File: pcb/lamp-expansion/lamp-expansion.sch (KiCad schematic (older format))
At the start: 87 parts, among them IC1 PAM2421, IC2 MCP73811, IC3 AP2401, IC6 LM1117_5.0, IC7 FT230X_SOP, IC9 CC3000, J1 MICROUSB, J10 CC-IO, J2 DCIN, J3 SERIAL, J4 5PIN_INPUT, J5 2PIN_POWER, J6 2PIN_IO, J7 2PIN_POWER, J8 AVR_ISP, J9 UF.L, Q1 2N7002

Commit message: board layout and schematic refinement
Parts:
- removed C10, C2: 0.1uF, symbol C
- removed IC3: AP2401, symbol AP24x1
- removed J10: CC-IO, symbol 3PIN_FEMALE
- removed J6: 2PIN_IO, symbol 2PIN_FEMALE
- removed R1: 10kΩ, symbol R
- removed TP11, TP12: PIN, symbol TEST
- added Q?: AO3415, symbol P-CHAN-MOSFET_SOT
- added R?: 100kΩ, symbol R
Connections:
- net labels removed: +BATT, AVR_0, AVR_1
- wire segments 255 -> 305
- no-connect marks 4 -> 3
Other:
- note added: "communication headers"
- note removed: "battery and charger"
- note removed: "buttons and pots header"
- note removed: "extra io"
- note removed: "power switch"
- note removed: "wifi io pins"
- moved on the sheet: BT1, C1, C9, D1, IC2, J4, R10, R11, S1, S2, TP10, TP6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

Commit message: a little more room fort activities
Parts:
- removed D1: 3A, symbol D_SCHOTTKY
- removed JP2: I-TEST, symbol JUMPER_2-PIN
- removed Q?: AO3415, symbol P-CHAN-MOSFET_SOT
- added IC3: NTHD3101F, symbol NTHD3101F
- gave numbers to parts that had none: 1
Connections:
- net +5V: now also IC3.1 (A), IC3.2 (A), IC3.4 (G)
- net VSUP: now also IC3.3 (S), IC3.7 (C), IC3.8 (C)
- net at BT1.1 (+), C9.1, IC2.3 (VBAT): now also IC3.5 (D), IC3.6 (D)
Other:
- moved on the sheet: J7, R1

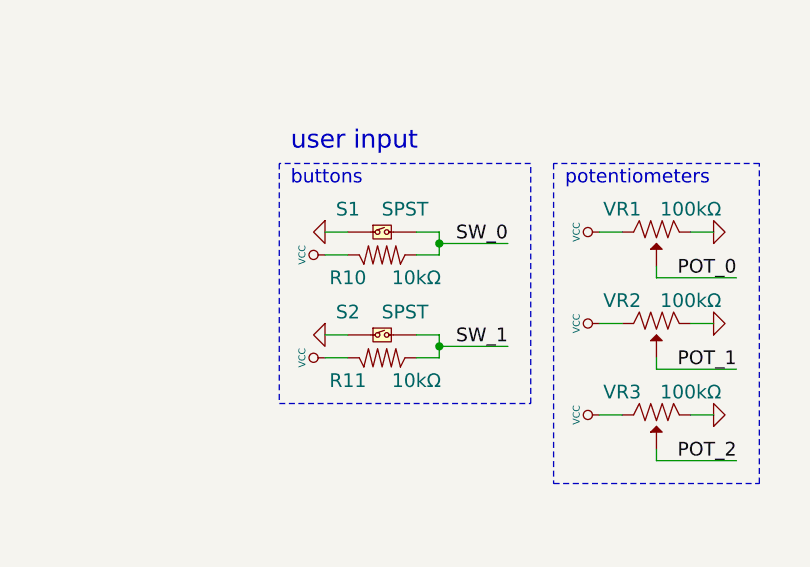
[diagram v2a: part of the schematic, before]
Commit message: layout and schematic refinements
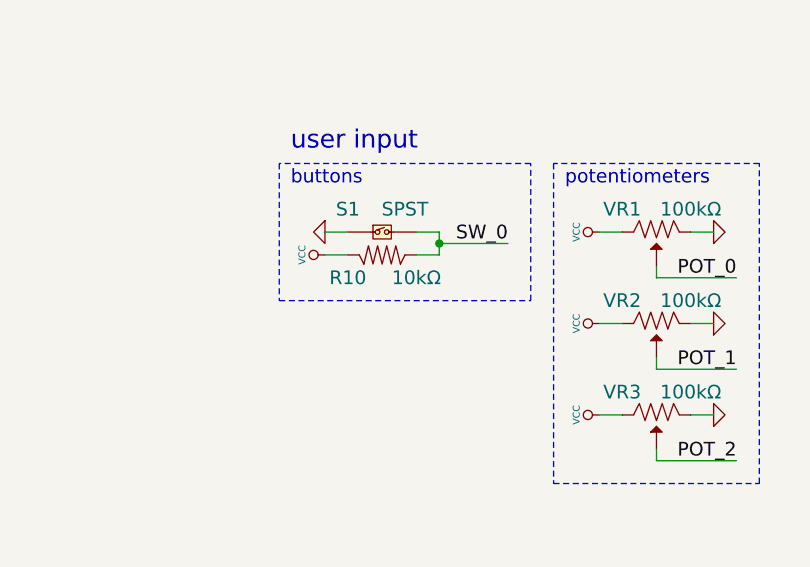
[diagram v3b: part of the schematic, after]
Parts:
- removed R11: 10kΩ, symbol R
- removed S2: SPST, symbol SPST
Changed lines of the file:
@@
 Text Label 8200 3700 2    60   ~ 0
 SW_0
-$Comp
-L SPST S2
-U 1 1 5358ABCF
-P 7650 4100
-F 0 "S2" H 7500 4200 60  0000 C CNN
-F 1 "SPST" H 7750 4200 60  0000 C CNN
-F 2 "" H 7650 4100 60  0001 C CNN
-F 3 "" H 7650 4100 60  0001 C CNN
-	1    7650 4100
-	1    0    0    -1
-$EndComp
-$Comp
-L GND #PWR046
-U 1 1 5358ABD5
-P 7400 4100
-F 0 "#PWR046" H 7400 4100 30  0001 C CNN
-F 1 "GND" H 7400 4030 30  0001 C CNN
-F 2 "" H 7400 4100 60  0000 C CNN
-F 3 "" H 7400 4100 60  0000 C CNN
-	1    7400 4100
-	0    1    1    0
-$EndComp
-$Comp
-L R R11
-U 1 1 5358ABDC
-P 7650 4200
-F 0 "R11" H 7500 4100 60  0000 C CNN
-F 1 "10kΩ" H 7800 4100 60  0000 C CNN
-F 2 "" H 7650 4200 60  0001 C CNN
-F 3 "" H 7650 4200 60  0001 C CNN
-	1    7650 4200
-	1    0    0    -1
-$EndComp
-$Comp
-L VCC #PWR047
-U 1 1 5358ABE2
-P 7400 4200
-F 0 "#PWR047" H 7400 4300 30  0001 C CNN
-F 1 "VCC" H 7400 4300 30  0000 C CNN
-F 2 "" H 7400 4200 60  0000 C CNN
-F 3 "" H 7400 4200 60  0000 C CNN
-	1    7400 4200
-	0    -1   -1   0
-$EndComp
-Text Label 8200 4150 2    60   ~ 0
-SW_1
 Text Notes 8450 3450 0    60   ~ 0
 potentiometers
@@
 $EndComp
 $Comp
-L PWR_FLAG #FLG048
+L PWR_FLAG #FLG046
 U 1 1 53613807
 P 3150 8950
-F 0 "#FLG048" H 3150 9045 30  0001 C CNN
+F 0 "#FLG046" H 3150 9045 30  0001 C CNN
 F 1 "PWR_FLAG" H 3150 9130 30  0000 C CNN
 F 2 "" H 3150 8950 60  0000 C CNN
@@
 $EndComp
 $Comp
-L PWR_FLAG #FLG049
+L PWR_FLAG #FLG047
 U 1 1 53613C3F
 P 7950 1550
-F 0 "#FLG049" H 7950 1645 30  0001 C CNN
+F 0 "#FLG047" H 7950 1645 30  0001 C CNN
 F 1 "PWR_FLAG" H 7950 1730 30  0000 C CNN
 F 2 "" H 7950 1550 60  0000 C CNN
@@
 $EndComp
 $Comp
-L PWR_FLAG #FLG050
+L PWR_FLAG #FLG048
 U 1 1 5361446B
 P 1900 4500
-F 0 "#FLG050" H 1900 4595 30  0001 C CNN
+F 0 "#FLG048" H 1900 4595 30  0001 C CNN
 F 1 "PWR_FLAG" H 1900 4680 30  0000 C CNN
 F 2 "" H 1900 4500 60  0000 C CNN
@@
 $EndComp
 $Comp
-L GND #PWR051
+L GND #PWR049
 U 1 1 5363359C
 P 2150 6550
-F 0 "#PWR051" H 2150 6550 30  0001 C CNN
+F 0 "#PWR049" H 2150 6550 30  0001 C CNN
 F 1 "GND" H 2150 6480 30  0001 C CNN
 F 2 "" H 2150 6550 60  0000 C CNN
@@
 $EndComp
 $Comp
-L GND #PWR052
+L GND #PWR050
 U 1 1 53634DCF
 P 1950 7150
-F 0 "#PWR052" H 1950 7150 30  0001 C CNN
+F 0 "#PWR050" H 1950 7150 30  0001 C CNN
 F 1 "GND" H 1950 7080 30  0001 C CNN
 F 2 "" H 1950 7150 60  0000 C CNN
@@
 $EndComp
 $Comp
-L GND #PWR053
+L GND #PWR051
 U 1 1 53635854
 P 2300 7550
-F 0 "#PWR053" H 2300 7550 30  0001 C CNN
+F 0 "#PWR051" H 2300 7550 30  0001 C CNN
 F 1 "GND" H 2300 7480 30  0001 C CNN
 F 2 "" H 2300 7550 60  0000 C CNN
@@
 $EndComp
 $Comp
-L GND #PWR054
+L GND #PWR052
 U 1 1 53635980
 P 3100 7550
-F 0 "#PWR054" H 3100 7550 30  0001 C CNN
+F 0 "#PWR052" H 3100 7550 30  0001 C CNN
 F 1 "GND" H 3100 7480 30  0001 C CNN
 F 2 "" H 3100 7550 60  0000 C CNN
@@
 $EndComp
 $Comp
-L GND #PWR055
+L GND #PWR053
 U 1 1 536399D8
 P 3900 6750
-F 0 "#PWR055" H 3900 6750 30  0001 C CNN
+F 0 "#PWR053" H 3900 6750 30  0001 C CNN
 F 1 "GND" H 3900 6680 30  0001 C CNN
 F 2 "" H 3900 6750 60  0000 C CNN
@@
 $EndComp
 $Comp
-L GND #PWR056
+L GND #PWR054
 U 1 1 5363BCDD
 P 3600 7150
-F 0 "#PWR056" H 3600 7150 30  0001 C CNN
+F 0 "#PWR054" H 3600 7150 30  0001 C CNN
 F 1 "GND" H 3600 7080 30  0001 C CNN
 F 2 "" H 3600 7150 60  0000 C CNN
@@
 $EndComp
 $Comp
-L GND #PWR057
+L GND #PWR055
 U 1 1 5363C419
 P 1400 6250
-F 0 "#PWR057" H 1400 6250 30  0001 C CNN
+F 0 "#PWR055" H 1400 6250 30  0001 C CNN
 F 1 "GND" H 1400 6180 30  0001 C CNN
 F 2 "" H 1400 6250 60  0000 C CNN
@@
 	7900 3650 7900 3750
 Connection ~ 7900 3700
-Wire Wire Line
-	7400 4100 7500 4100
-Wire Wire Line
-	7400 4200 7500 4200
-Wire Wire Line
-	8200 4150 7900 4150
-Wire Wire Line
-	7900 4100 7800 4100
-Wire Wire Line
-	7900 4200 7800 4200
-Wire Wire Line
-	7900 4100 7900 4200
-Connection ~ 7900 4150
 Wire Notes Line
 	8400 3350 8400 4750
@@
 	9300 3350 8400 3350
 Wire Notes Line
-	7200 3350 7200 4400
-Wire Notes Line
-	7200 4400 8300 4400
-Wire Notes Line
-	8300 4400 8300 3350
+	7200 3350 7200 3950
+Wire Notes Line
+	7200 3950 8300 3950
+Wire Notes Line
+	8300 3950 8300 3350
 Wire Notes Line
 	8300 3350 7200 3350
@@
 	5300 7000 5200 7000
 $Comp
-L VCC #PWR058
+L VCC #PWR056
 U 1 1 53649906
 P 14700 4100
-F 0 "#PWR058" H 14700 4200 30  0001 C CNN
+F 0 "#PWR056" H 14700 4200 30  0001 C CNN
 F 1 "VCC" H 14700 4200 30  0000 C CNN
 F 2 "" H 14700 4100 60  0000 C CNN
@@
 NoConn ~ 11600 6200
 $Comp
-L GND #PWR059
+L GND #PWR057
 U 1 1 5364A71C
 P 12600 6200
-F 0 "#PWR059" H 12600 6200 30  0001 C CNN
+F 0 "#PWR057" H 12600 6200 30  0001 C CNN
 F 1 "GND" H 12600 6130 30  0001 C CNN
 F 2 "" H 12600 6200 60  0000 C CNN
@@
 $EndComp
 $Comp
-L PWR_FLAG #FLG060
+L PWR_FLAG #FLG058
 U 1 1 5364FF84
 P 3050 4850
-F 0 "#FLG060" H 3050 4945 30  0001 C CNN
+F 0 "#FLG058" H 3050 4945 30  0001 C CNN
 F 1 "PWR_FLAG" H 3050 5030 30  0000 C CNN
 F 2 "" H 3050 4850 60  0000 C CNN
@@
 Connection ~ 3050 4750
 $Comp
-L PWR_FLAG #FLG061
+L PWR_FLAG #FLG059
 U 1 1 53651E8C
 P 7250 9600
-F 0 "#FLG061" H 7250 9695 30  0001 C CNN
+F 0 "#FLG059" H 7250 9695 30  0001 C CNN
 F 1 "PWR_FLAG" H 7250 9780 30  0000 C CNN
 F 2 "" H 7250 9600 60  0000 C CNN
@@
 $EndComp
 $Comp
-L PWR_FLAG #FLG062
+L PWR_FLAG #FLG060
 U 1 1 536B0BCA
 P 9200 1550
-F 0 "#FLG062" H 9200 1645 30  0001 C CNN
+F 0 "#FLG060" H 9200 1645 30  0001 C CNN
 F 1 "PWR_FLAG" H 9200 1730 30  0000 C CNN
 F 2 "" H 9200 1550 60  0000 C CNN
@@
 $EndComp
 $Comp
-L +5V #PWR063
+L +5V #PWR061
 U 1 1 536ABC20
 P 3850 2150
-F 0 "#PWR063" H 3850 2240 20  0001 C CNN
+F 0 "#PWR061" H 3850 2240 20  0001 C CNN
 F 1 "+5V" H 3850 2240 30  0000 C CNN
 F 2 "" H 3850 2150 60  0000 C CNN
@@
 Connection ~ 3800 2150
 $Comp
-L +5V #PWR064
+L +5V #PWR062
 U 1 1 536AC23F
 P 3850 1600
-F 0 "#PWR064" H 3850 1690 20  0001 C CNN
+F 0 "#PWR062" H 3850 1690 20  0001 C CNN
 F 1 "+5V" H 3850 1690 30  0000 C CNN
 F 2 "" H 3850 1600 60  0000 C CNN
@@
 	3700 1900 4100 1900
 $Comp
-L GND #PWR065
+L GND #PWR063
 U 1 1 536AD142
 P 3300 1600
-F 0 "#PWR065" H 3300 1600 30  0001 C CNN
+F 0 "#PWR063" H 3300 1600 30  0001 C CNN
 F 1 "GND" H 3300 1530 30  0001 C CNN
 F 2 "" H 3300 1600 60  0000 C CNN

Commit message: still working on the layout
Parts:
- VR1, VR2, VR3: Distrib. Part (none) -> PTA2043-2015CPB103-ND; Distributor (none) -> Digikey; Manuf. Part (none) -> PTA2043-2015CPB103; Manufacturer (none) -> Bourns

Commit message: add changes found after first iMac powerup since 2014
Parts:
- AE1: footprint (none) -> johanson:JOHANSON-2500AT44M0400_2.4GHz-chip-antenna
- BT1: footprint (none) -> connect-thru:JST-S2B-PH-K_right-angle-jack
- C1, C14, C15, C16, C18, C22, C24, C26, C27, C28, C29, C30, C4, C5, C6, C9, L2, L3, R1, R10, R12, R13, R2, R4, R5, R6, R7, R8, R9: footprint (none) -> passive-smd:0603(1608m)
- C13, C20, C31, C7, C8, F1: footprint (none) -> passive-smd:1206(3216m)
- C19, C3: footprint (none) -> capacitor:PANA-D_CHEMI-F_SM-ALUMINUM
- D2, D6: footprint (none) -> diode:MICROSMP
- D3, D4: footprint (none) -> diode:DO-214AC
- IC1: footprint (none) -> sop:SOP8_ep
- IC2: footprint (none) -> sot:SOT23-5
- IC3: footprint (none) -> sot:CHIPFET-1206-8
- IC6: footprint (none) -> sot:SOT223
- IC7: footprint (none) -> sop:SSOP16
- IC9: footprint (none) -> texas:CC3000
- J1: footprint (none) -> connect-sm:MICROUSB_sm
- J2: footprint (none) -> connect-thru:CUI-PJ-102A_dc-barrel-jack
- J3: footprint (none) -> sip:SIP6
- J4: footprint (none) -> sip:SIP5
- J5, J7: footprint (none) -> sip:SIP2
- J8: footprint (none) -> connect-thru:2x3-ARRAY_P100mil
- J9: footprint (none) -> connect-sm:U.FL-COAX
- JP3: footprint (none) -> jumper:SOLDER-JUMPER_2-WAY
- L1: footprint (none) -> inductor:SM-INDUCTOR_6mmX6mm
- LED1, LED2: footprint (none) -> led:0603(1608m)-SM-LED
- Q1: footprint (none) -> sot:SOT23; Manuf. Part 2N7002P,215 -> 2N7002P
- R3: footprint (none) -> passive-smd:0603(1608m); Manufacturer (none) -> something
- S1: footprint (none) -> switch:SPST-2-PIN_6mm_thru
- TP1, TP10, TP2, TP3, TP4, TP5, TP6, TP7, TP8, TP9: footprint (none) -> connect-thru:1-PIN
- VR1, VR2, VR3: footprint (none) -> bourns:BOURNS-PTA2043_20mm-slide-pot
